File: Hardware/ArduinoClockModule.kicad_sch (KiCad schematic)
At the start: 38 parts, among them J1 AudioJack2_SwitchT, J2 AudioJack2_SwitchT, J3 AudioJack2_SwitchT, J4 AudioJack2_SwitchT, J5 Conn_02x05_Odd_Even, SW1 SW_Push, SW2 SW_Push, SW3 RotaryEncoder_Switch, U1 LM324, U4 74HC595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

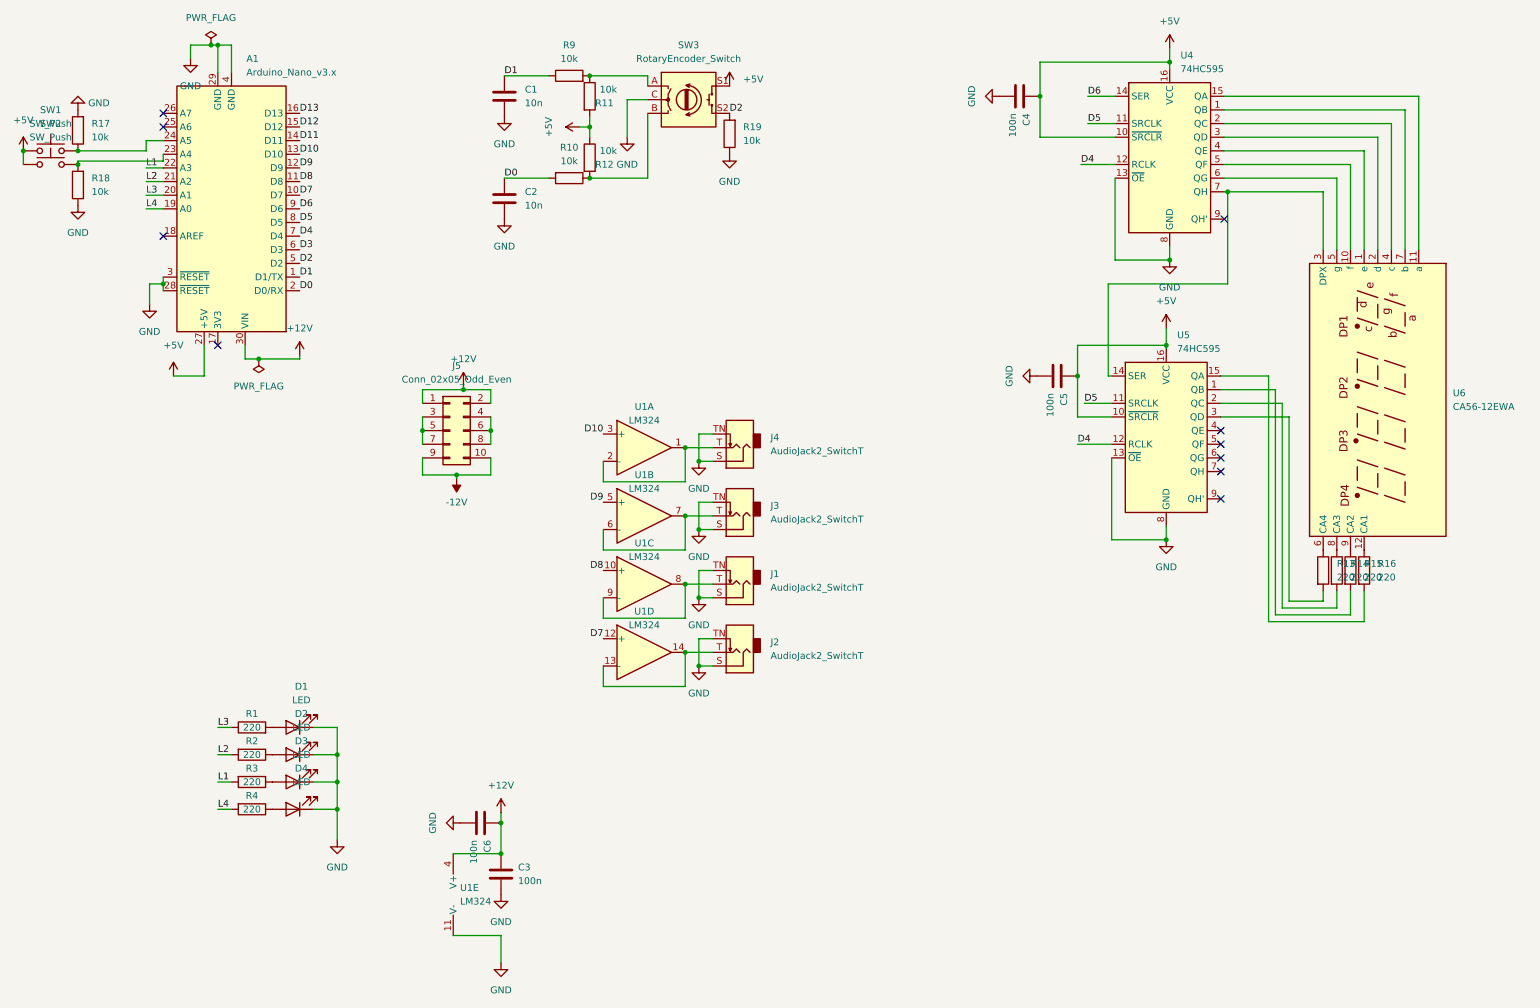
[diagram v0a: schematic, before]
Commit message: First working protorype. The class should allow some expansion of features wihtout too major refactors. Some modifications to the hardware is still needed.
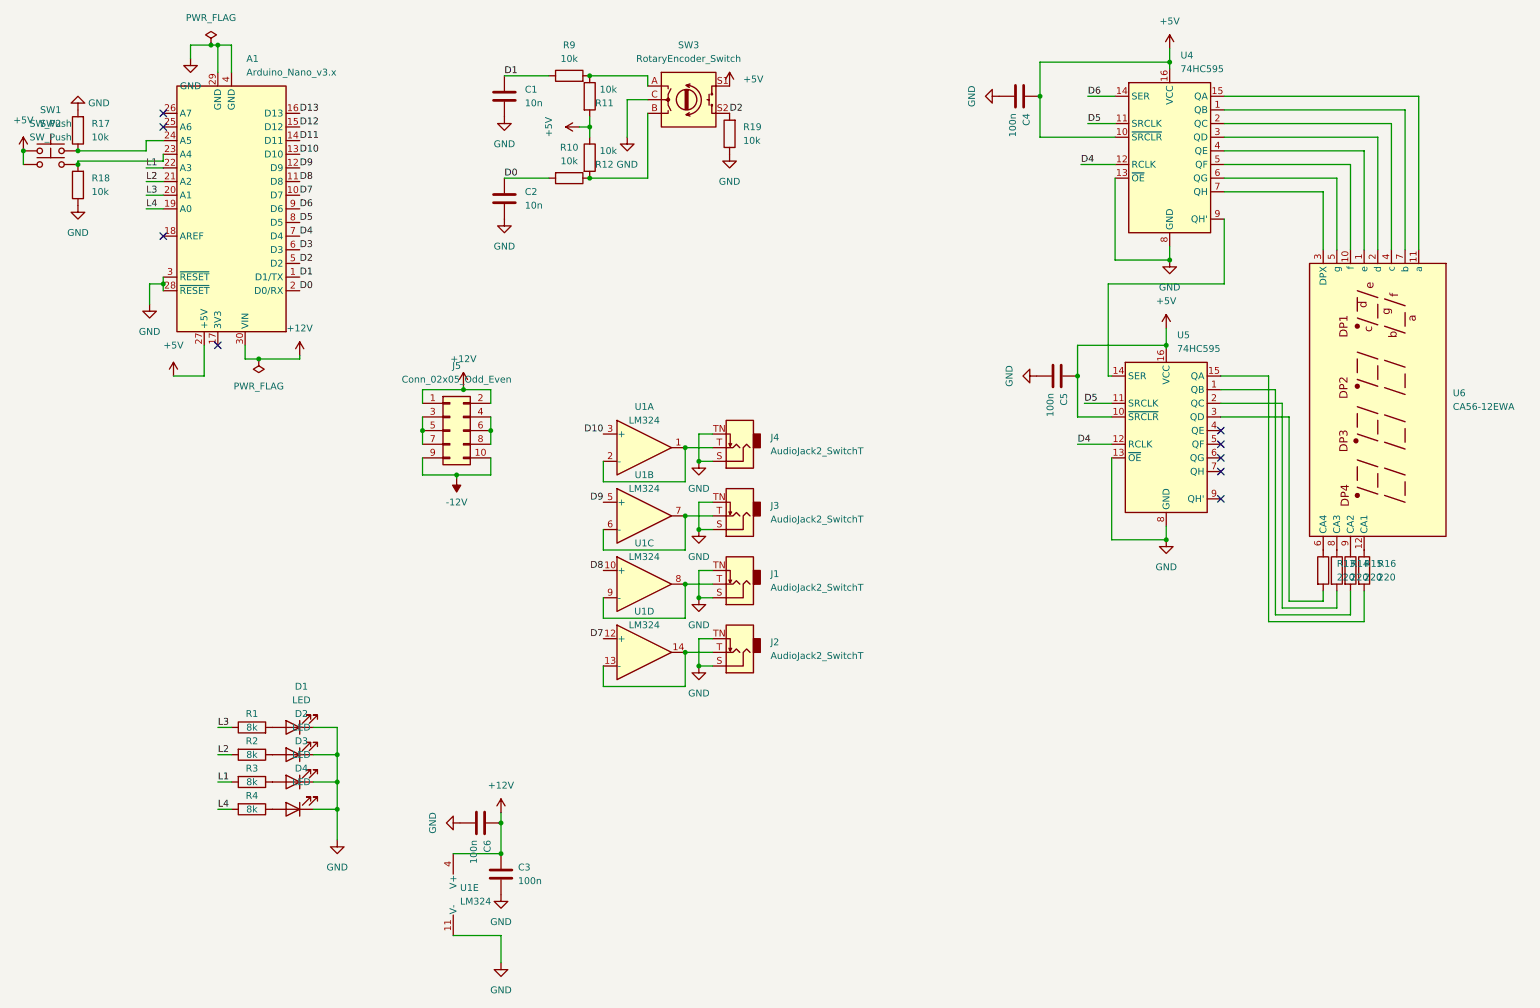
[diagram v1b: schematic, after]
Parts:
- R1, R2, R3, R4: value 220 -> 8k
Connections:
- net at U4.7 (QH), U6.3 (DPX): no longer U5.14 (SER)
- net at U4.9 (QH'): now also U5.14 (SER)
- no-connect marks 10 -> 9
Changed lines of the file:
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@@
   (junction (at 76.835 152.4) (diameter 0) (color 0 0 0 0)
-  )
-  (junction (at 242.57 47.625) (diameter 0) (color 0 0 0 0)
   )
   (junction (at 231.775 23.495) (diameter 0) (color 0 0 0 0)
@@
   (no_connect (at 241.3 99.695))
   (no_connect (at 241.3 94.615))
-  (no_connect (at 241.935 52.705))
   (no_connect (at 44.45 35.56))
   (no_connect (at 241.3 92.075))
@@
     (stroke (width 0) (type default) (color 0 0 0 0))
   )
-  (wire (pts (xy 242.57 64.77) (xy 220.345 64.77))
-    (stroke (width 0) (type default) (color 0 0 0 0))
-  )
   (wire (pts (xy 76.835 152.4) (xy 76.835 157.48))
     (stroke (width 0) (type default) (color 0 0 0 0))
@@
     (stroke (width 0) (type default) (color 0 0 0 0))
   )
-  (wire (pts (xy 260.35 47.625) (xy 242.57 47.625))
+  (wire (pts (xy 241.935 47.625) (xy 260.35 47.625))
     (stroke (width 0) (type default) (color 0 0 0 0))
   )
@@
     (stroke (width 0) (type default) (color 0 0 0 0))
   )
-  (wire (pts (xy 241.935 47.625) (xy 242.57 47.625))
-    (stroke (width 0) (type default) (color 0 0 0 0))
-  )
   (wire (pts (xy 231.14 109.855) (xy 231.14 112.395))
     (stroke (width 0) (type default) (color 0 0 0 0))
@@
     (stroke (width 0) (type default) (color 0 0 0 0))
   )
+  (wire (pts (xy 220.345 64.77) (xy 241.935 64.77))
+    (stroke (width 0) (type default) (color 0 0 0 0))
+  )
   (wire (pts (xy 144.145 97.79) (xy 146.685 97.79))
     (stroke (width 0) (type default) (color 0 0 0 0))
@@
     (stroke (width 0) (type default) (color 0 0 0 0))
   )
-  (wire (pts (xy 242.57 47.625) (xy 242.57 64.77))
-    (stroke (width 0) (type default) (color 0 0 0 0))
-  )
   (wire (pts (xy 130.81 30.48) (xy 130.81 37.465))
     (stroke (width 0) (type default) (color 0 0 0 0))
@@
   )
   (wire (pts (xy 105.41 97.155) (xy 105.41 100.33))
+    (stroke (width 0) (type default) (color 0 0 0 0))
+  )
+  (wire (pts (xy 241.935 52.705) (xy 241.935 64.77))
     (stroke (width 0) (type default) (color 0 0 0 0))
   )
@@
     (in_bom yes) (on_board yes)
     (property "Reference" "R3" (id 0) (at 60.96 154.94 90))
-    (property "Value" "220" (id 1) (at 60.96 157.48 90))
+    (property "Value" "8k" (id 1) (at 60.96 157.48 90))
     (property "Footprint" "Resistor_THT:R_Axial_DIN0207_L6.3mm_D2.5mm_P7.62mm_Horizontal" (id 2) (at 60.96 155.702 90)
       (effects (font (size 1.27 1.27)) hide)
@@
     (in_bom yes) (on_board yes)
     (property "Reference" "R1" (id 0) (at 60.96 144.78 90))
-    (property "Value" "220" (id 1) (at 60.96 147.32 90))
+    (property "Value" "8k" (id 1) (at 60.96 147.32 90))
     (property "Footprint" "Resistor_THT:R_Axial_DIN0207_L6.3mm_D2.5mm_P7.62mm_Horizontal" (id 2) (at 60.96 149.098 90)
       (effects (font (size 1.27 1.27)) hide)
@@
     (in_bom yes) (on_board yes)
     (property "Reference" "R4" (id 0) (at 60.96 160.02 90))
-    (property "Value" "220" (id 1) (at 60.96 162.56 90))
+    (property "Value" "8k" (id 1) (at 60.96 162.56 90))
     (property "Footprint" "Resistor_THT:R_Axial_DIN0207_L6.3mm_D2.5mm_P7.62mm_Horizontal" (id 2) (at 60.96 160.782 90)
       (effects (font (size 1.27 1.27)) hide)
@@
     (in_bom yes) (on_board yes)
     (property "Reference" "R2" (id 0) (at 60.96 149.86 90))
-    (property "Value" "220" (id 1) (at 60.96 152.4 90))
+    (property "Value" "8k" (id 1) (at 60.96 152.4 90))
     (property "Footprint" "Resistor_THT:R_Axial_DIN0207_L6.3mm_D2.5mm_P7.62mm_Horizontal" (id 2) (at 60.96 150.622 90)
       (effects (font (size 1.27 1.27)) hide)
@@
     )
     (path "/5677780a-7328-4853-b1d7-43c7bb82c73a"
-      (reference "R1") (unit 1) (value "220") (footprint "Resistor_THT:R_Axial_DIN0207_L6.3mm_D2.5mm_P7.62mm_Horizontal")
+      (reference "R1") (unit 1) (value "8k") (footprint "Resistor_THT:R_Axial_DIN0207_L6.3mm_D2.5mm_P7.62mm_Horizontal")
     )
     (path "/fa69a8f6-7ecb-4327-8574-4176e64f01b6"
-      (reference "R2") (unit 1) (value "220") (footprint "Resistor_THT:R_Axial_DIN0207_L6.3mm_D2.5mm_P7.62mm_Horizontal")
+      (reference "R2") (unit 1) (value "8k") (footprint "Resistor_THT:R_Axial_DIN0207_L6.3mm_D2.5mm_P7.62mm_Horizontal")
     )
     (path "/509ab011-e22a-4568-aef4-6d737a409684"
-      (reference "R3") (unit 1) (value "220") (footprint "Resistor_THT:R_Axial_DIN0207_L6.3mm_D2.5mm_P7.62mm_Horizontal")
+      (reference "R3") (unit 1) (value "8k") (footprint "Resistor_THT:R_Axial_DIN0207_L6.3mm_D2.5mm_P7.62mm_Horizontal")
     )
     (path "/7792cc5c-9f6e-4789-8a85-36ff672e1e8a"
-      (reference "R4") (unit 1) (value "220") (footprint "Resistor_THT:R_Axial_DIN0207_L6.3mm_D2.5mm_P7.62mm_Horizontal")
+      (reference "R4") (unit 1) (value "8k") (footprint "Resistor_THT:R_Axial_DIN0207_L6.3mm_D2.5mm_P7.62mm_Horizontal")
     )
     (path "/712f2d65-b949-49f7-ad55-40c2393e14b5"
